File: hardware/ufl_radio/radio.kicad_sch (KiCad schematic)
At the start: 29 parts, among them J4 Shield, J5 U.FL, U3 MAX2769B

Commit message: Slight cleanup
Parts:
- C16: LCSC (none) -> C1525
- C17, C19, C26: LCSC (none) -> C307449
- C20: LCSC (none) -> C15195
- C23: LCSC (none) -> C1557
- R16: LCSC (none) -> C25765
- R4: LCSC C25900 -> C11702
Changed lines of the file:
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@@
+			)
+		)
+		(property "LCSC" "C25765"
+			(at 193.04 100.33 90)
+			(effects
+				(font
+					(size 1.27 1.27)
+				)
+				(hide yes)
 			)
 		)
@@
 			)
 		)
-		(property "LCSC" "C25900"
+		(property "LCSC" "C11702"
 			(at 26.035 107.9499 0)
 			(effects
@@
 			)
 		)
-		(property "LCSC" "C25900"
+		(property "LCSC" "C11702"
 			(at 40.005 107.9499 0)
 			(effects
@@
 			)
 		)
+		(property "LCSC" "C1525"
+			(at 93.98 91.44 0)
+			(effects
+				(font
+					(size 1.27 1.27)
+				)
+				(hide yes)
+			)
+		)
 		(pin "1"
 		)
@@
 			)
 		)
+		(property "LCSC" "C15195"
+			(at 147.32 72.39 0)
+			(effects
+				(font
+					(size 1.27 1.27)
+				)
+				(hide yes)
+			)
+		)
 		(pin "1"
 		)
@@
 			)
 		)
+		(property "LCSC" "C307449"
+			(at 134.62 156.21 90)
+			(effects
+				(font
+					(size 1.27 1.27)
+				)
+				(hide yes)
+			)
+		)
 		(pin "1"
 		)
@@
 			)
 		)
+		(property "LCSC" "C307449"
+			(at 100.33 104.14 90)
+			(effects
+				(font
+					(size 1.27 1.27)
+				)
+				(hide yes)
+			)
+		)
 		(pin "1"
 		)
@@
 			)
 		)
+		(property "LCSC" "C1557"
+			(at 184.15 104.14 0)
+			(effects
+				(font
+					(size 1.27 1.27)
+				)
+				(hide yes)
+			)
+		)
 		(pin "1"
 		)
@@
 			)
 		)
+		(property "LCSC" "C307449"
+			(at 204.47 104.14 0)
+			(effects
+				(font
+					(size 1.27 1.27)
+				)
+				(hide yes)
+			)
+		)
 		(pin "1"
 		)
@@
 			)
 		)
-		(property "LCSC" "C25900"
+		(property "LCSC" "C11702"
 			(at 53.975 107.9499 0)
 			(effects

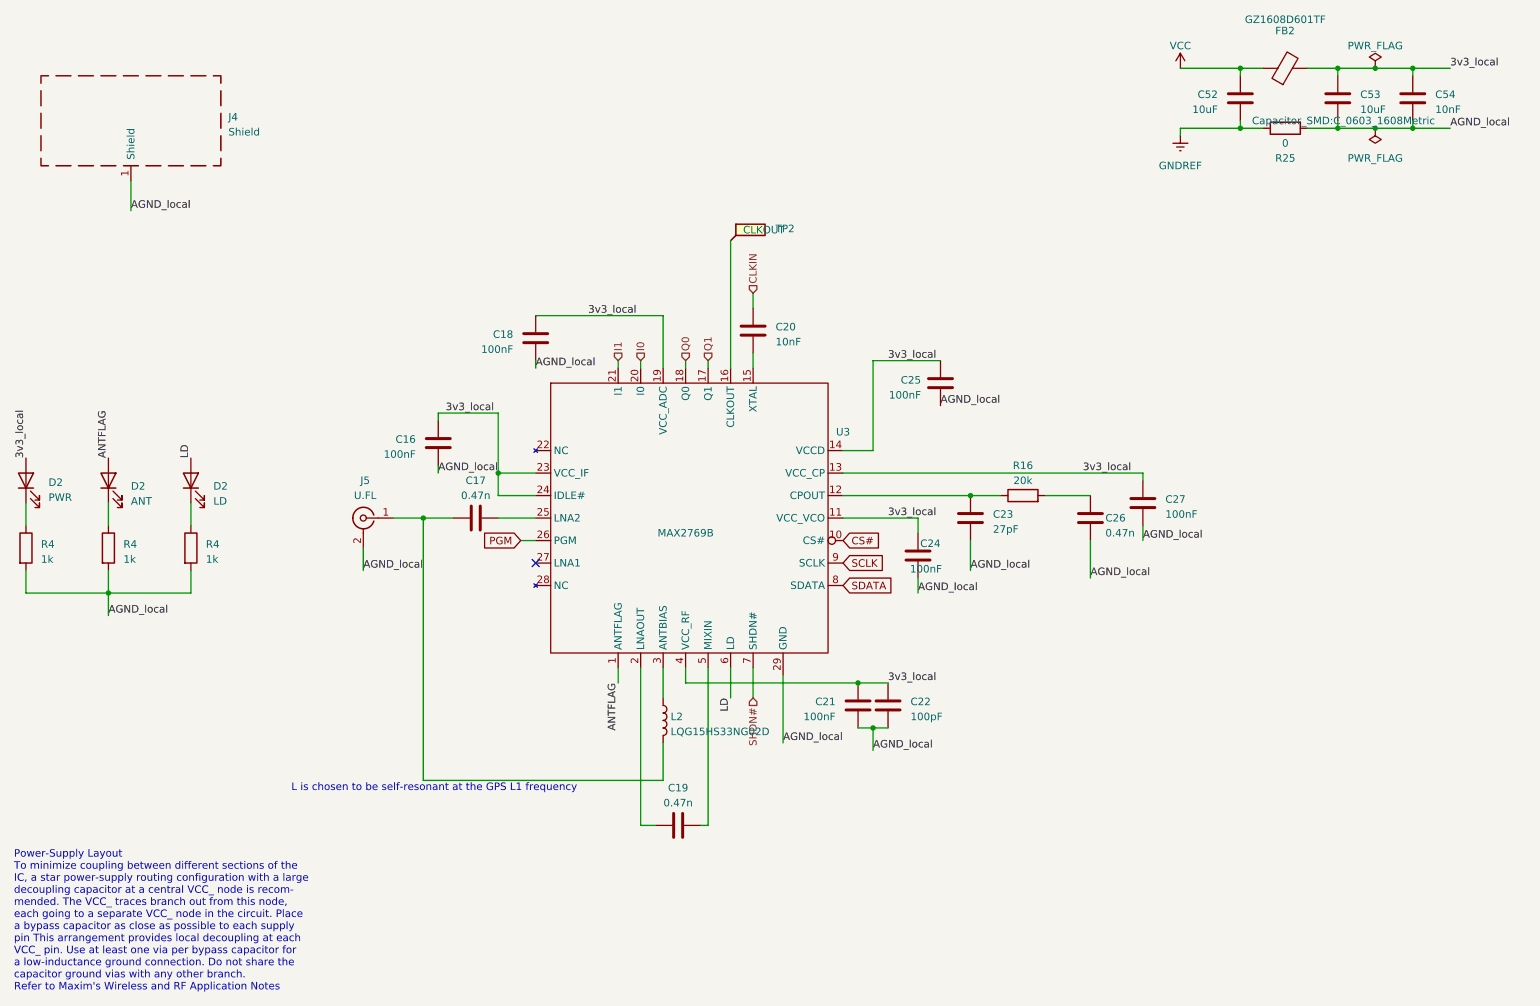
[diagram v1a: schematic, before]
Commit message: Move to kicad 9. Add panelization script and basic instructions
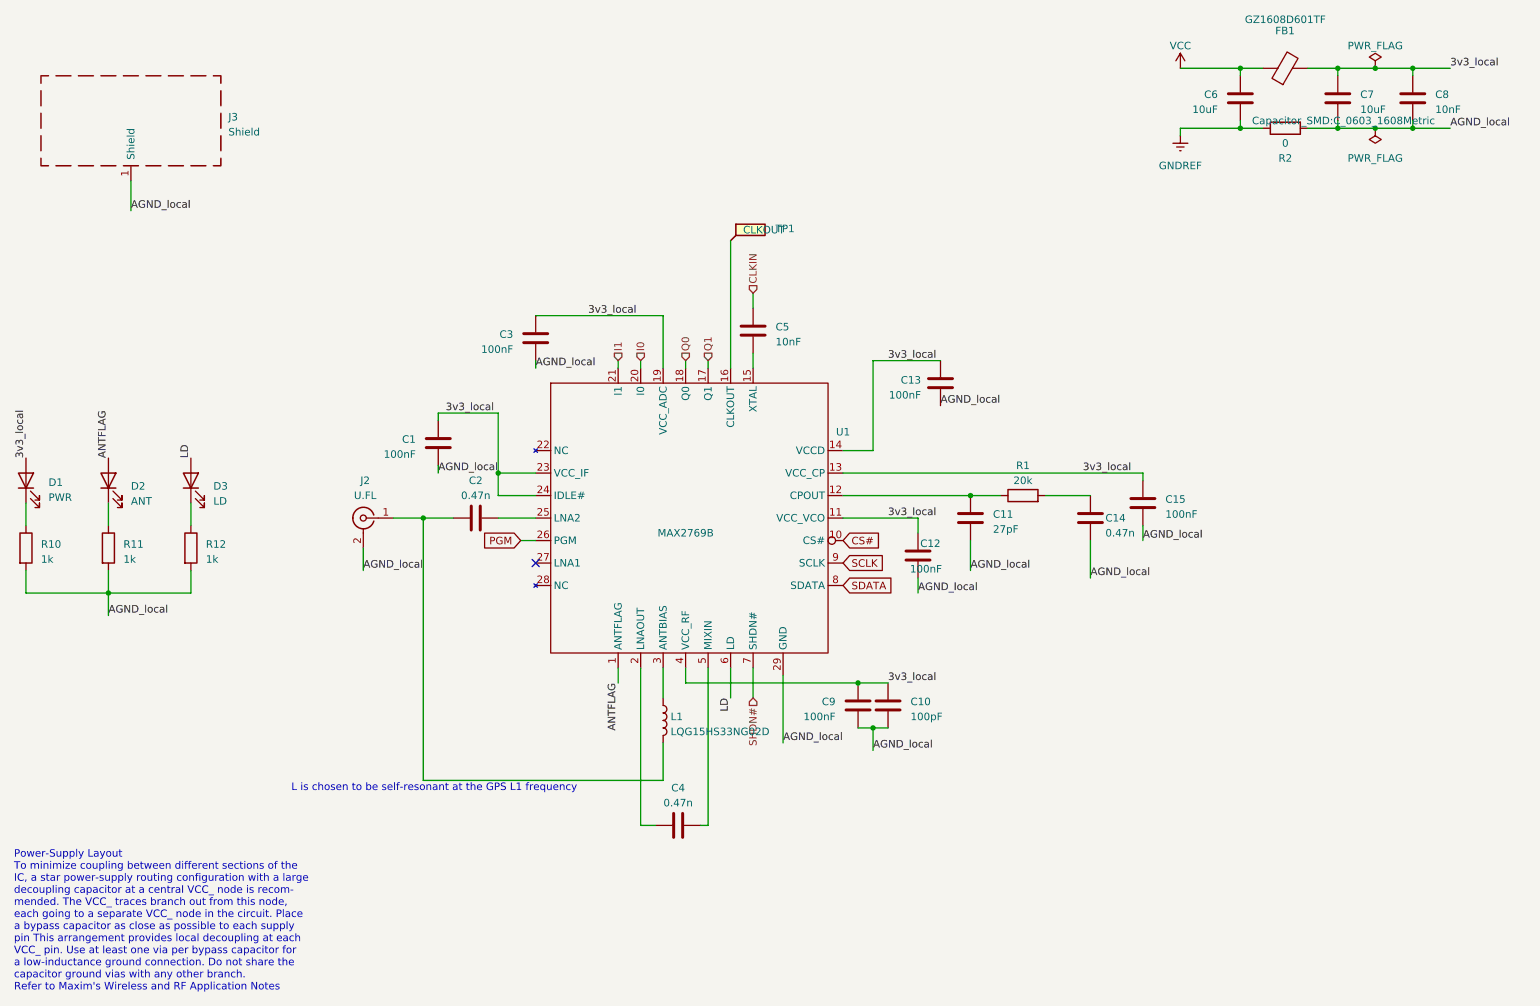
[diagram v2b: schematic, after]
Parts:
- renumbered C16 to C1, C22 to C10, C23 to C11, C24 to C12, C25 to C13, C26 to C14, C27 to C15, C17 to C2, C18 to C3, C19 to C4, C20 to C5, C52 to C6, C53 to C7, C54 to C8, C21 to C9, D2 to D1, D2 to D3, FB2 to FB1, J5 to J2, J4 to J3, L2 to L1, R16 to R1, R4 to R10, R4 to R11, R4 to R12, R25 to R2, TP2 to TP1, U3 to U1
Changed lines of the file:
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@@
 (kicad_sch
-	(version 20231120)
+	(version 20250114)
 	(generator "eeschema")
-	(generator_version "8.0")
+	(generator_version "9.0")
 	(paper "A4")
+	(text "L is chosen to be self-resonant at the GPS L1 frequency"
+		(exclude_from_sim no)
+		(at 69.088 150.622 0)
+		(effects
+			(font
+				(size 1.27 1.27)
+			)
+			(justify left bottom)
+		)
+	)
+	(text "Power-Supply Layout\nTo minimize coupling between different sections of the\nIC, a star power-supply routing configuration with a large\ndecoupling capacitor at a central VCC_ node is recom-\nmended. The VCC_ traces branch out from this node,\neach going to a separate VCC_ node in the circuit. Place\na bypass capacitor as close as possible to each supply\npin This arrangement provides local decoupling at each\nVCC_ pin. Use at least one via per bypass capacitor for\na low-inductance ground connection. Do not share the\ncapacitor ground vias with any other branch.\nRefer to Maxim's Wireless and RF Application Notes\n"
+		(exclude_from_sim no)
+		(at 22.098 184.404 0)
+		(effects
+			(font
+				(size 1.27 1.27)
+			)
+			(justify left bottom)
+		)
+	)
 	(junction
 		(at 167.64 139.7)
@@
 		)
 	)
-	(text "L is chosen to be self-resonant at the GPS L1 frequency"
-		(exclude_from_sim no)
-		(at 69.088 150.622 0)
-		(effects
-			(font
-				(size 1.27 1.27)
-			)
-			(justify left bottom)
-		)
-	)
-	(text "Power-Supply Layout\nTo minimize coupling between different sections of the\nIC, a star power-supply routing configuration with a large\ndecoupling capacitor at a central VCC_ node is recom-\nmended. The VCC_ traces branch out from this node,\neach going to a separate VCC_ node in the circuit. Place\na bypass capacitor as close as possible to each supply\npin This arrangement provides local decoupling at each\nVCC_ pin. Use at least one via per bypass capacitor for\na low-inductance ground connection. Do not share the\ncapacitor ground vias with any other branch.\nRefer to Maxim's Wireless and RF Application Notes\n"
-		(exclude_from_sim no)
-		(at 22.098 184.404 0)
-		(effects
-			(font
-				(size 1.27 1.27)
-			)
-			(justify left bottom)
-		)
-	)
 	(label "LD"
 		(at 143.51 134.62 270)
-		(fields_autoplaced yes)
 		(effects
 			(font
@@
 	(label "3v3_local"
 		(at 170.18 132.08 0)
-		(fields_autoplaced yes)
 		(effects
 			(font
@@
 	(label "AGND_local"
 		(at 41.91 52.07 0)
-		(fields_autoplaced yes)
 		(effects
 			(font
@@
 	(label "3v3_local"
 		(at 203.2 96.52 0)
-		(fields_autoplaced yes)
 		(effects
 			(font
@@
 	(label "LD"
 		(at 52.07 93.98 90)
-		(fields_autoplaced yes)
 		(effects
 			(font
@@
 	(label "3v3_local"
 		(at 170.18 104.14 0)
-		(fields_autoplaced yes)
 		(effects
 			(font
@@
 	(label "AGND_local"
 		(at 184.15 113.03 0)
-		(fields_autoplaced yes)
 		(effects
 			(font
@@
 	(label "AGND_local"
 		(at 93.98 96.52 0)
-		(fields_autoplaced yes)
 		(effects
 			(font
@@
 	(label "ANTFLAG"
 		(at 38.1 93.98 90)
-		(fields_autoplaced yes)
 		(effects
 			(font
@@
 	(label "AGND_local"
 		(at 110.49 78.74 0)
-		(fields_autoplaced yes)
 		(effects
 			(font
@@
 	(label "ANTFLAG"
 		(at 124.46 132.08 270)
-		(fields_autoplaced yes)
 		(effects
 			(font
@@
 	(label "AGND_local"
 		(at 204.47 114.3 0)
-		(fields_autoplaced yes)
 		(effects
 			(font
@@
 	(label "AGND_local"
 		(at 179.07 85.09 0)
-		(fields_autoplaced yes)
 		(effects
 			(font
@@
 	(label "3v3_local"
 		(at 170.18 77.47 0)
-		(fields_autoplaced yes)
 		(effects
 			(font
@@
 	(label "AGND_local"
 		(at 38.1 120.65 0)
-		(fields_autoplaced yes)
 		(effects
 			(font
@@
 	(label "3v3_local"
 		(at 265.43 27.94 0)
-		(fields_autoplaced yes)
 		(effects
 			(font
@@
 	(label "3v3_local"
 		(at 95.25 86.36 0)
-		(fields_autoplaced yes)
 		(effects
 			(font
@@
 	(label "AGND_local"
 		(at 175.26 116.84 0)
-		(fields_autoplaced yes)
 		(effects
 			(font
@@
 	(label "AGND_local"
 		(at 152.4 142.24 0)
-		(fields_autoplaced yes)
 		(effects
 			(font
@@
 	(label "AGND_local"
 		(at 213.36 107.95 0)
-		(fields_autoplaced yes)
 		(effects
 			(font
@@
 	(label "AGND_local"
 		(at 81.28 113.03 0)
-		(fields_autoplaced yes)
 		(effects
 			(font
@@
 	(label "3v3_local"
 		(at 119.38 69.85 0)
-		(fields_autoplaced yes)
 		(effects
 			(font
@@
 	(label "AGND_local"
 		(at 265.43 38.1 0)
-		(fields_autoplaced yes)
 		(effects
 			(font
@@
 	(label "AGND_local"
 		(at 167.64 143.51 0)
-		(fields_autoplaced yes)
 		(effects
 			(font
@@
 	(label "3v3_local"
 		(at 24.13 93.98 90)
-		(fields_autoplaced yes)
 		(effects
 			(font
@@
 		(shape input)
 		(at 124.46 77.47 90)
-		(fields_autoplaced yes)
 		(effects
 			(font
@@
 		(shape input)
 		(at 135.89 77.47 90)
-		(fields_autoplaced yes)
 		(effects
 			(font
@@
 		(shape input)
 		(at 147.32 134.62 270)
-		(fields_autoplaced yes)
 		(effects
 			(font
@@
 		(shape input)
 		(at 147.32 66.04 90)
-		(fields_autoplaced yes)
 		(effects
 			(font
@@
 		(shape input)
 		(at 139.7 77.47 90)
-		(fields_autoplaced yes)
 		(effects
 			(font
@@
 		(shape input)
 		(at 128.27 77.47 90)
-		(fields_autoplaced yes)
 		(effects
 			(font
@@
 		(dnp no)
 		(fields_autoplaced yes)
-		(property "Reference" "J5"
+		(property "Reference" "J2"
 			(at 81.5974 97.79 0)
 			(effects
@@
 		(dnp no)
 		(fields_autoplaced yes)
-		(property "Reference" "R16"
+		(property "Reference" "R1"
 			(at 193.04 95.25 90)
 			(effects
@@
 		(on_board yes)
 		(dnp no)
-		(property "Reference" "C18"
+		(property "Reference" "C3"
 			(at 106.68 73.025 0)
 			(effects
@@
 		(dnp no)
 		(fields_autoplaced yes)
-		(property "Reference" "R4"
+		(property "Reference" "R10"
 			(at 26.67 108.585 0)
 			(effects
@@
 		(dnp no)
 		(fields_autoplaced yes)
-		(property "Reference" "R4"
+		(property "Reference" "R11"
 			(at 40.64 108.585 0)
 			(effects
@@
 		(on_board yes)
 		(dnp no)
-		(property "Reference" "R25"
+		(property "Reference" "R2"
 			(at 237.49 43.18 90)
 			(effects
@@
 		(dnp no)
 		(fields_autoplaced yes)
-		(property "Reference" "#FLG07"
+		(property "Reference" "#FLG03"
 			(at 252.73 26.035 0)
 			(effects
@@
 		(dnp no)
 		(fields_autoplaced yes)
-		(property "Reference" "L2"
+		(property "Reference" "L1"
 			(at 133.35 137.795 0)
 			(effects
@@
 		(on_board yes)
 		(dnp no)
-		(property "Reference" "C16"
+		(property "Reference" "C1"
 			(at 90.17 90.805 0)
 			(effects
@@
 		(dnp no)
 		(fields_autoplaced yes)
-		(property "Reference" "D2"
+		(property "Reference" "D1"
 			(at 27.94 98.1074 90)
 			(effects
@@
 		(dnp no)
 		(fields_autoplaced yes)
-		(property "Reference" "C20"
+		(property "Reference" "C5"
 			(at 151.13 71.755 0)
 			(effects
@@
 		(on_board yes)
 		(dnp no)
-		(property "Reference" "C52"
+		(property "Reference" "C6"
 			(at 226.06 32.385 0)
 			(effects
@@
 		(on_board yes)
 		(dnp no)
-		(property "Reference" "C24"
+		(property "Reference" "C12"
 			(at 179.07 108.458 0)
 			(effects
@@
 		(dnp no)
 		(fields_autoplaced yes)
-		(property "Reference" "C19"
+		(property "Reference" "C4"
 			(at 134.62 149.86 90)
 			(effects
@@
 		(dnp no)
 		(fields_autoplaced yes)
-		(property "Reference" "C17"
+		(property "Reference" "C2"
 			(at 100.33 97.79 90)
 			(effects
@@
 		(dnp no)
 		(fields_autoplaced yes)
-		(property "Reference" "J4"
+		(property "Reference" "J3"
 			(at 58.42 36.195 0)
 			(effects
@@
 		(on_board yes)
 		(dnp no)
-		(property "Reference" "C21"
+		(property "Reference" "C9"
 			(at 161.29 135.255 0)
 			(effects
@@
 		(on_board yes)
 		(dnp no)
-		(property "Reference" "U3"
+		(property "Reference" "U1"
 			(at 162.56 89.5603 0)
 			(effects
@@
 		(on_board yes)
 		(dnp no)
-		(property "Reference" "C27"
+		(property "Reference" "C15"
 			(at 217.17 100.965 0)
 			(effects
@@
 		(dnp no)
 		(fields_autoplaced yes)
-		(property "Reference" "#PWR085"
+		(property "Reference" "#PWR03"
 			(at 219.71 31.75 0)
 			(effects
@@
 		(on_board yes)
 		(dnp no)
-		(property "Reference" "FB2"
+		(property "Reference" "FB1"
 			(at 237.4392 21.59 90)
 			(effects
@@
 		(dnp no)
 		(fields_autoplaced yes)
-		(property "Reference" "C23"
+		(property "Reference" "C11"
 			(at 187.96 103.505 0)
 			(effects
@@
 		(dnp no)
 		(fields_autoplaced yes)
-		(property "Reference" "C22"
+		(property "Reference" "C10"
 			(at 173.99 135.255 0)
 			(effects
@@
 		(dnp no)
 		(fields_autoplaced yes)
-		(property "Reference" "#FLG08"
+		(property "Reference" "#FLG04"
 			(at 252.73 40.005 0)
 			(effects
@@
 		(on_board yes)
 		(dnp no)
-		(property "Reference" "C26"
+		(property "Reference" "C14"
 			(at 207.01 104.14 0)
 			(effects
@@
 		(dnp no)
 		(fields_autoplaced yes)
-		(property "Reference" "C53"
+		(property "Reference" "C7"
 			(at 250.19 32.385 0)
 			(effects
@@
 		(on_board yes)
 		(dnp no)
-		(property "Reference" "TP2"
+		(property "Reference" "TP1"
 			(at 151.13 55.118 0)
 			(effects
@@
 		(dnp no)
 		(fields_autoplaced yes)
-		(property "Reference" "R4"
+		(property "Reference" "R12"
 			(at 54.61 108.585 0)
 			(effects
@@
 		(dnp no)
 		(fields_autoplaced yes)
-		(property "Reference" "D2"
+		(property "Reference" "D3"
 			(at 55.88 98.7425 90)
 			(effects
@@
 		(on_board yes)
 		(dnp no)
-		(property "Reference" "C25"
+		(property "Reference" "C13"
 			(at 175.768 80.772 0)
 			(effects
@@
 		(dnp no)
 		(fields_autoplaced yes)
-		(property "Reference" "C54"
+		(property "Reference" "C8"
 			(at 262.89 32.385 0)
 			(effects
@@
 		(dnp no)
 		(fields_autoplaced yes)
-		(property "Reference" "#PWR086"
+		(property "Reference" "#PWR04"
 			(at 219.71 45.72 0)
 			(effects

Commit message: Nearly ready
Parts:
- J3: LCSC (none) -> C7469751; NOTE (none) -> Using TE Connectivity MFR.Part # 2118706-2; now in the parts list
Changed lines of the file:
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@@
 		(unit 1)
 		(exclude_from_sim no)
-		(in_bom no)
-		(on_board no)
+		(in_bom yes)
+		(on_board yes)
 		(dnp no)
 		(fields_autoplaced yes)
@@
 			(at 41.91 36.83 0)
 			(effects
+				(font
+					(size 1.27 1.27)
+				)
+				(hide yes)
+			)
+		)
+		(property "LCSC" "C7469751"
+			(at 41.91 36.83 0)
+			(effects
+				(font
+					(size 1.27 1.27)
+				)
+				(hide yes)
+			)
+		)
+		(property "NOTE" "Using TE Connectivity MFR.Part # 2118706-2"
+			(at 41.91 36.83 0)
+			(effects

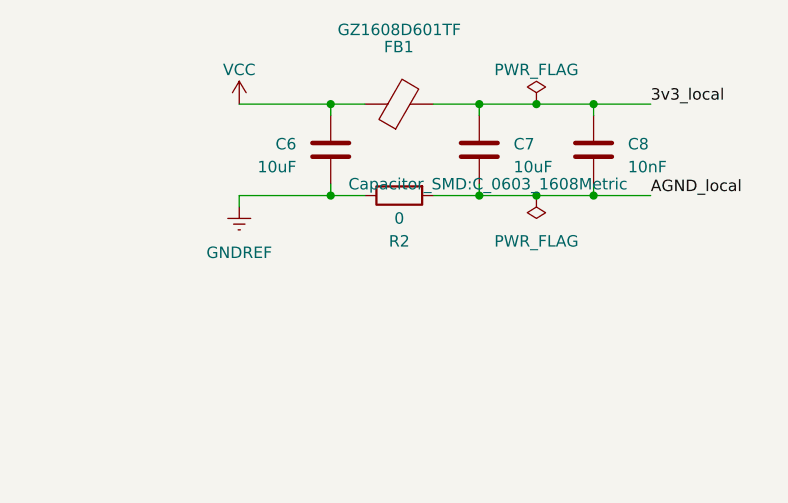
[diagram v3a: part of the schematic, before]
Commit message: Fix up ground rules
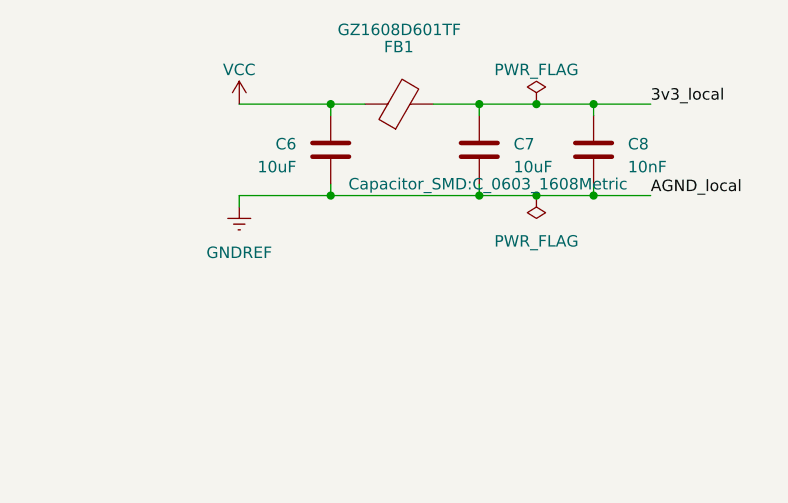
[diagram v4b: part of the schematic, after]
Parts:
- removed R2: 0, Resistor_SMD:R_0402_1005Metric, symbol Device:R
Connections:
- net AGND_local is gone; now on net GNDREF: C1.2, C10.2, C11.1, C12.2, C13.2, C14.2, C15.2, C3.2, C7.2, C8.2, C9.2, J2.2 (Ext), J3.1 (Shield), R10.2, R11.2, R12.2, U1.29 (GND)
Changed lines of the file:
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@@
-	(wire
-		(pts
-			(xy 241.3 38.1) (xy 246.38 38.1)
-		)
-		(stroke
-			(width 0)
-			(type default)
-		)
-	)
 	(wire
 		(pts
@@
 	(wire
 		(pts
-			(xy 229.87 38.1) (xy 233.68 38.1)
+			(xy 229.87 38.1) (xy 246.38 38.1)
 		)
 		(stroke
@@
 					(unit 1)
 				)
-			)
-		)
-	)
-	(symbol
-		(lib_id "Device:R")
-		(at 237.49 38.1 90)
-		(mirror x)
-		(unit 1)
-		(exclude_from_sim no)
-		(in_bom yes)
-		(on_board yes)
-		(dnp no)
-		(property "Reference" "R2"
-			(at 237.49 43.18 90)
-			(effects
-				(font
-					(size 1.27 1.27)
-				)
-			)
-		)
-		(property "Value" "0"
-			(at 237.49 40.64 90)
-			(effects
-				(font
-					(size 1.27 1.27)
-				)
-			)
-		)
-		(property "Footprint" "Resistor_SMD:R_0402_1005Metric"
-			(at 237.49 36.322 90)
-			(effects
-				(font
-					(size 1.27 1.27)
-				)
-				(hide yes)
-			)
-		)
-		(property "Datasheet" "~"
-			(at 237.49 38.1 0)
-			(effects
-				(font
-					(size 1.27 1.27)
-				)
-				(hide yes)
-			)
-		)
-		(property "Description" "Resistor"
-			(at 237.49 38.1 0)
-			(effects
-				(font
-					(size 1.27 1.27)
-				)
-				(hide yes)
-			)
-		)
-		(property "LCSC" "C17168"
-			(at 237.49 38.1 90)
-			(effects
-				(font
-					(size 1.27 1.27)
-				)
-				(hide yes)
-			)
-		)
-		(pin "1"
-		)
-		(pin "2"
-		)
-		(instances
-			(project "design"
-				(path "/6dbd6c42-edf6-461d-b7ca-066e49b0019c/1b895c4a-56fd-4590-a8aa-7507dccb37cf"
-					(reference "R25")
-					(unit 1)
-				)
-				(path "/6dbd6c42-edf6-461d-b7ca-066e49b0019c/78691f3e-c8cc-4de2-b4f7-4d5d660bca23"
-					(reference "R2")
-					(unit 1)
-				)
-				(path "/6dbd6c42-edf6-461d-b7ca-066e49b0019c/bbad701b-ab9c-48bf-af04-0d262cb749b1"
-					(reference "R26")
-					(unit 1)
-				)
-				(path "/6dbd6c42-edf6-461d-b7ca-066e49b0019c/f20fbf31-47b8-4912-9caa-c1ed256d71c4"
-					(reference "R27")
-					(unit 1)
-				)
